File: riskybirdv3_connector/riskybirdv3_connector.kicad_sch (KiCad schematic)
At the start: 74 parts, among them J1 USB_C_Receptacle_USB2.0_16P, J2 USB_C_Receptacle_USB2.0_16P, J3 Conn_02x10_Odd_Even, J4 USB_C_Receptacle_PowerOnly_6P, J7 Conn_01x02, U1 AP2112K-3.3, U15 FT2232HL-REEL, U2 AP2112K-3.3, U4 MCP73831-2-OT, U9 FT2232HL-REEL, Y2 f, Y3 f

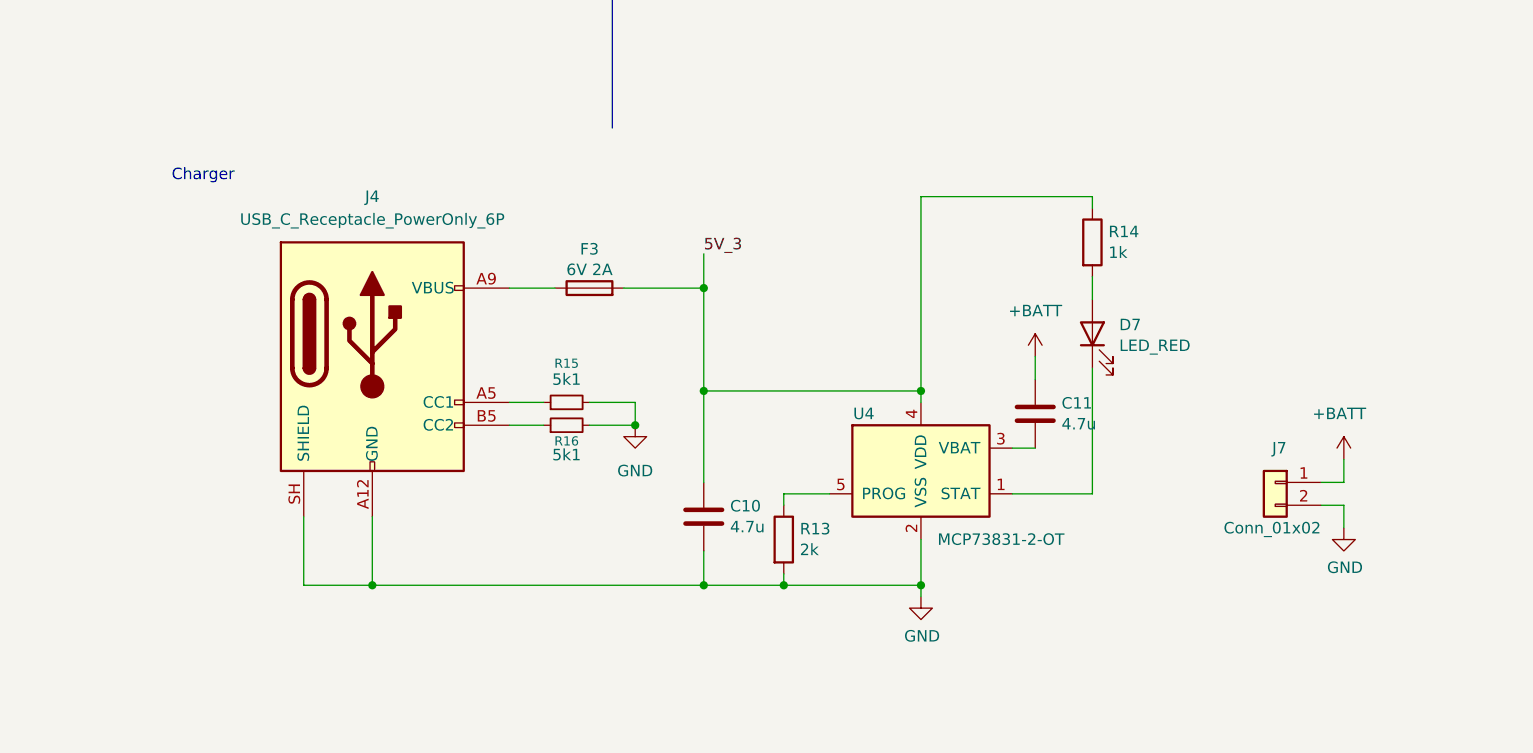
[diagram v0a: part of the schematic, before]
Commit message: remove: charger, kept on main board
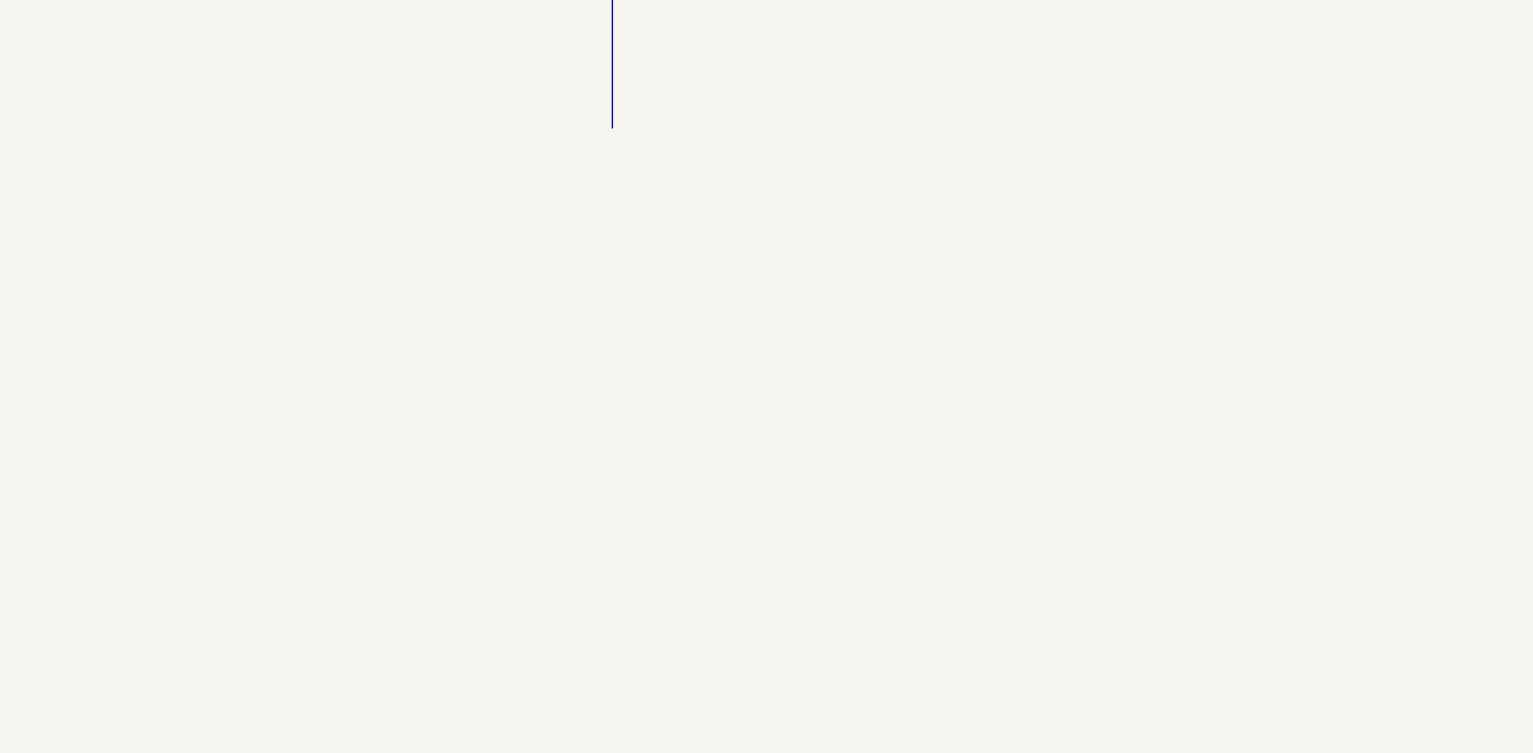
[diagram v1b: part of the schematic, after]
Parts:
- removed C10, C11: 4.7u, Capacitor_SMD:C_0201_0603Metric, symbol Device:C
- removed D7: LED_RED, LED_SMD:LED_0402_1005Metric, symbol Device:LED
- removed F3: 6V 2A, symbol Device:Fuse
- removed J4: USB_C_Receptacle_PowerOnly_6P, symbol Connector:USB_C_Receptacle_PowerOnly_6P
- removed J7: Conn_01x02, Connector_PinHeader_2.00mm:PinHeader_1x02_P2.00mm_Vertical, symbol Connector_Generic:Conn_01x02
- removed R13: 2k, Resistor_SMD:R_0201_0603Metric, symbol Device:R
- removed R14: 1k, Resistor_SMD:R_0201_0603Metric, symbol Device:R
- removed R15, R16: 5k1, symbol Device:R_Small
- removed U4: MCP73831-2-OT, Package_TO_SOT_SMD:SOT-23-5, symbol riskybird-rescue:MCP73831-2-OT-Battery_Management
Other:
- note removed: "Charger"

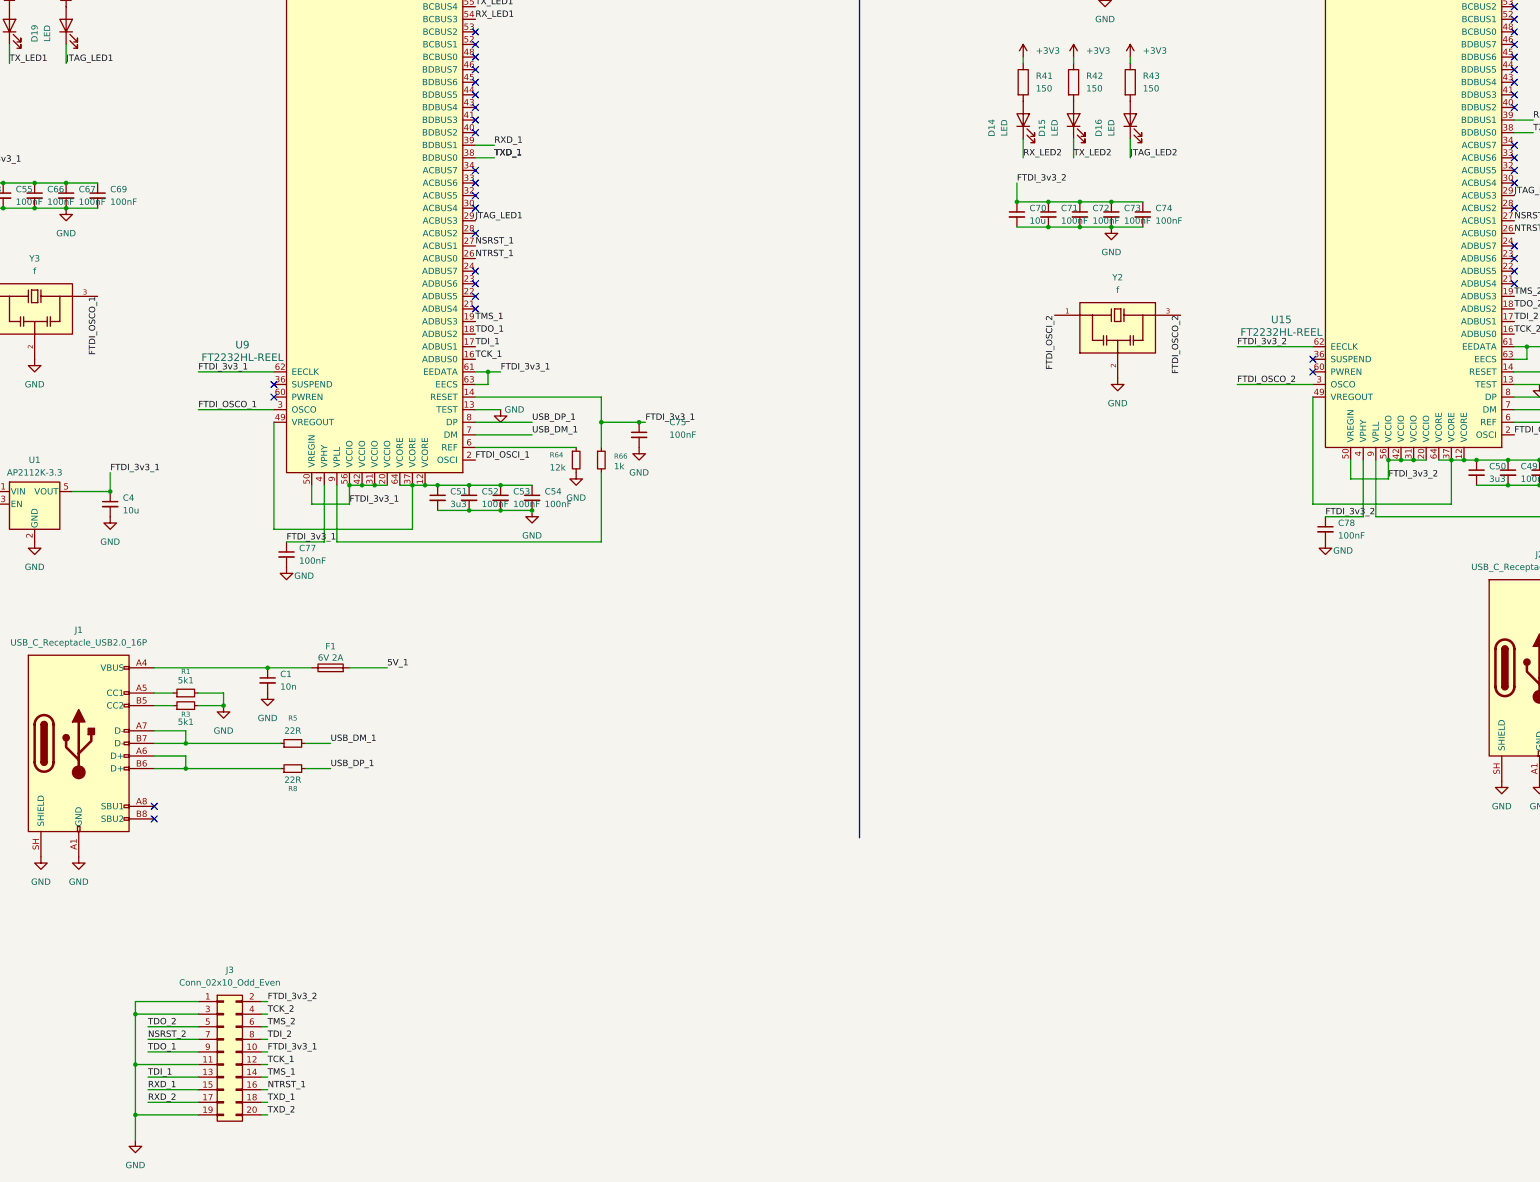
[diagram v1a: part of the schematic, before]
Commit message: add: missing footprints, VCCIO from b2b, and start layout
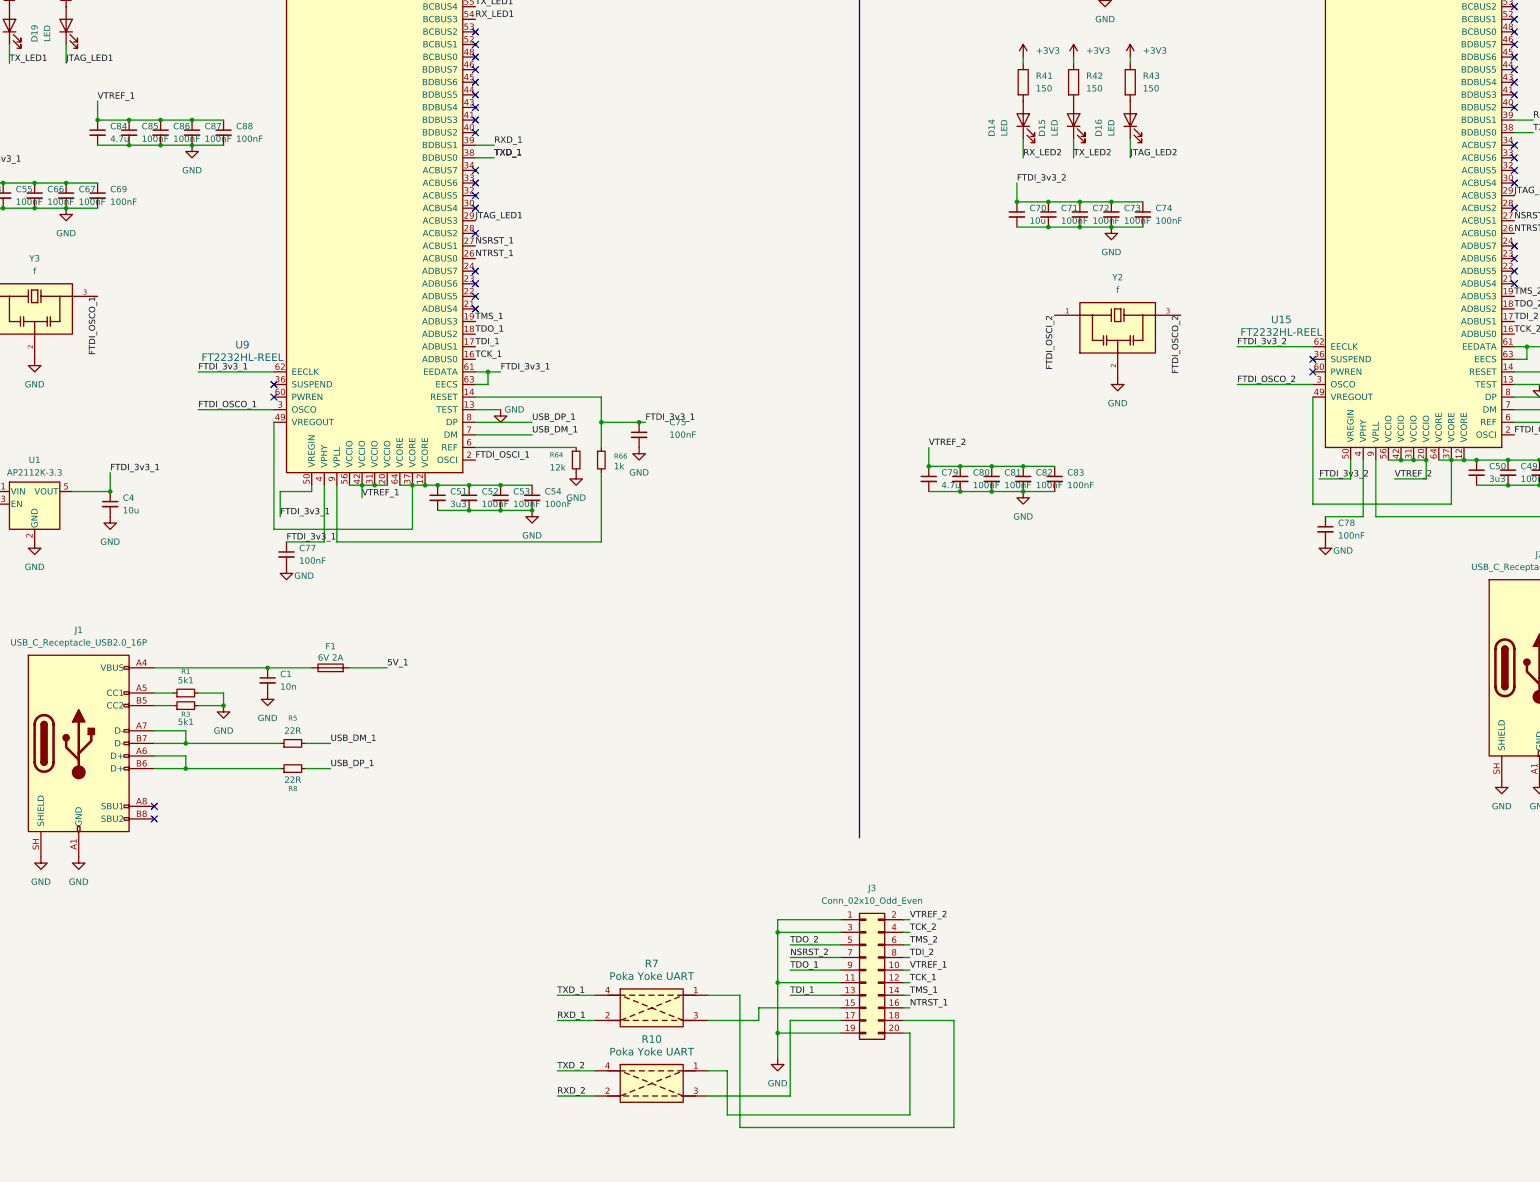
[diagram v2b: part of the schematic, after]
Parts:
- added C79, C84: 4.7u, Capacitor_SMD:C_0201_0603Metric, symbol Device:C_Small
- added C80, C81, C82, C83, C85, C86, C87, C88: 100nF, Capacitor_SMD:C_0201_0603Metric, symbol Device:C_Small
- added R10, R7: Poka Yoke UART, Resistor_SMD:poka_yoke_uart_SMD, symbol poka_yoke_uart:Poka Yoke UART
- C1, C2, C3, C4, C5, C6: footprint (none) -> Capacitor_SMD:C_0201_0603Metric
- F1, F2: footprint (none) -> Fuse:Fuse_1210_3225Metric
- J1, J2: footprint (none) -> Connector_USB:USB_C_Receptacle_GCT_USB4105-xx-A_16P_TopMnt_Horizontal
- R1, R2, R3, R4, R5, R6, R64, R65, R66, R67, R8, R9: footprint (none) -> Resistor_SMD:R_0201_0603Metric
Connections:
- net FTDI_3v3_1: no longer J3.10 (Pin_10), U9.20 (VCCIO), U9.31 (VCCIO), U9.42 (VCCIO), U9.56 (VCCIO)
- net FTDI_3v3_2: no longer C78.1, J3.2 (Pin_2), U15.20 (VCCIO), U15.31 (VCCIO), U15.4 (VPHY), U15.42 (VCCIO), U15.56 (VCCIO)
- net GND: now also C79.2, C80.2, C81.2, C82.2, C83.2, C84.2, C85.2, C86.2, C87.2, C88.2
- net RXD_1: now also R7.2; no longer J3.15 (Pin_15)
- net RXD_2: now also R10.2; no longer J3.17 (Pin_17)
- net TXD_1: now also R7.4; no longer J3.18 (Pin_18)
- net TXD_2: now also R10.4; no longer J3.20 (Pin_20)
- new net: C78.1, U15.4 (VPHY)
- new net: J3.15 (Pin_15), R7.3
- new net: J3.17 (Pin_17), R10.3
- new net: J3.18 (Pin_18), R7.1
- new net: J3.20 (Pin_20), R10.1
- new net VTREF_1: C84.1, C85.1, C86.1, C87.1, C88.1, J3.10 (Pin_10), U9.20 (VCCIO), U9.31 (VCCIO), U9.42 (VCCIO), U9.56 (VCCIO)
- new net VTREF_2: C79.1, C80.1, C81.1, C82.1, C83.1, J3.2 (Pin_2), U15.20 (VCCIO), U15.31 (VCCIO), U15.42 (VCCIO), U15.56 (VCCIO)
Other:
- moved on the sheet: J3

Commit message: add: layout backup
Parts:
- added TP12, TP13, TP14, TP16, TP17, TP18, TP19, TP20, TP22, TP23, TP24, TP25, TP27, TP28, TP29, TP30, TP32: TestPoint, TestPoint:TestPoint_Pad_D1.0mm, symbol Connector:TestPoint
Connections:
- net FTDI_3v3_1: now also R44.1, R49.1, R63.1, TP22.1
- net FTDI_3v3_2: now also C78.1, R41.1, R42.1, R43.1, U15.4 (VPHY), TP32.1
- net GND: now also TP17.1
- net RXD_1: now also TP18.1
- net RXD_2: now also TP28.1
- net TCK_1: now also TP13.1
- net TCK_2: now also TP24.1
- net TDI_1: now also TP14.1
- net TDI_2: now also TP25.1
- net TDO_1: now also TP20.1
- net TDO_2: now also TP30.1
- net TMS_1: now also TP19.1
- net TMS_2: now also TP29.1
- net TXD_1: now also TP12.1
- net TXD_2: now also TP23.1
- net VTREF_1: now also TP16.1
- net VTREF_2: now also TP27.1
- removed net +3V3: R41.1, R42.1, R43.1, R44.1, R49.1, R63.1
- net NSRST_1: no longer names the net of U9.27 (ACBUS1)
- net NTRST_2: no longer names the net of U15.26 (ACBUS0)
- no-connect marks 50 -> 52
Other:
- note added: "Ground"
- note added: "JTAG"
- note added: "Power Lines (FTDI & VTREF)"
- note added: "UART"

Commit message: add: saved changes
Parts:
- U15, U9: MANUFACTURER (none) -> FTDI, Future Technology Devices International Ltd; Manufacturer FTDI, Future Technology Devices International Ltd -> (none)

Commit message: riskybirdv3_connector: link all parts to JLC/LCSC + fix LED BOM/CPL desync
- Add LCSC Part + MPN/Manufacturer fields to all 73 sourceable components
  so JLC assembly matches by part number (no value-only footprint mismatch)
- Scale 10uF caps to fit 0201: C3/C5->2.2uF/10V (C319184),
  C4/C6/C68/C70->4.7uF (C335103); no PCB change
- Assign LED colors: JTAG=red (C130719), RX=yellow (C434450), TX=green (C434449)
- Set R7/R10 (Poka-Yoke UART keys) DNP -> hand-soldered
- Rename LED symbols D14-D19 -> functional refs JTAG1/RX1/TX1/JTAG2/RX2/TX2
  to match PCB footprint refs (silk), fixing BOM<->CPL designator mismatch
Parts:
- C1, C2: LCSC Part (none) -> C285010; MPN (none) -> 0201B103K250NT
- C3, C5: value 10u -> 2.2u; LCSC Part (none) -> C319184; MPN (none) -> GRM033R61A225ME47D
- C38, C39, C49, C52, C53, C54, C55, C66, C67, C69, C71, C72, C73, C74, C75, C76, C77, C78, C80, C81, C82, C83, C85, C86, C87, C88: LCSC Part (none) -> C76939; MPN (none) -> GRM033R61E104KE14D
- C4, C6, C68, C70: value 10u -> 4.7u; LCSC Part (none) -> C335103; MPN (none) -> GRM035R60J475ME15D
- C50, C51: LCSC Part (none) -> C514591; MPN (none) -> CL03A305MQ37RNZ
- C79, C84: LCSC Part (none) -> C335103; MPN (none) -> GRM035R60J475ME15D
- F1, F2: LCSC Part (none) -> C914221; MPN (none) -> BSMD1210-200-6V
- J1, J2: LCSC Part (none) -> C3025063; MPN (none) -> USB4105-GF-A-060
- J3: LCSC Part (none) -> C20728453; MPN (none) -> FTSH-110-01-L-DV-K-TR
- JTAG1: renamed from D19; value LED -> LED_Red; LCSC Part (none) -> C130719; MPN (none) -> NCD0402R1
- JTAG2: renamed from D16; value LED -> LED_Red; LCSC Part (none) -> C130719; MPN (none) -> NCD0402R1
- R1, R2, R3, R4: LCSC Part (none) -> C270344; MPN (none) -> 0201WMF5101TEE
- R41, R42, R43, R44, R49, R63: LCSC Part (none) -> C295773; MPN (none) -> RC0201FR-07150RL
- R5, R6, R8, R9: LCSC Part (none) -> C155743; MPN (none) -> RC0201FR-0722RL
- R64, R65: LCSC Part (none) -> C270363; MPN (none) -> 0201WMF1202TEE
- R66, R67: LCSC Part (none) -> C270365; MPN (none) -> 0201WMF1001TEE
- RX1: renamed from D17; value LED -> LED_Yellow; LCSC Part (none) -> C434450; MPN (none) -> SZYY0402Y
- RX2: renamed from D14; value LED -> LED_Yellow; LCSC Part (none) -> C434450; MPN (none) -> SZYY0402Y
- TX1: renamed from D18; value LED -> LED_Green; LCSC Part (none) -> C434449; MPN (none) -> SZYY0402YG
- TX2: renamed from D15; value LED -> LED_Green; LCSC Part (none) -> C434449; MPN (none) -> SZYY0402YG
- U1, U2: LCSC Part (none) -> C23380830; MPN (none) -> AP2112K-3.3TRG1
- U15, U9: LCSC Part (none) -> C27882
- Y2, Y3: LCSC Part (none) -> C341520; MPN (none) -> CSTNE12M0G550000R0
